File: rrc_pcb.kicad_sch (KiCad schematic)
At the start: 13 parts, among them J1 Conn_01x02_Male-Connector, J2 Conn_01x03_Male-Connector, U1 iridium9602, U2 Teensy4.1, U3 BN220-GPS, U4 ICM-20948, U5 MS5611, U6 logo

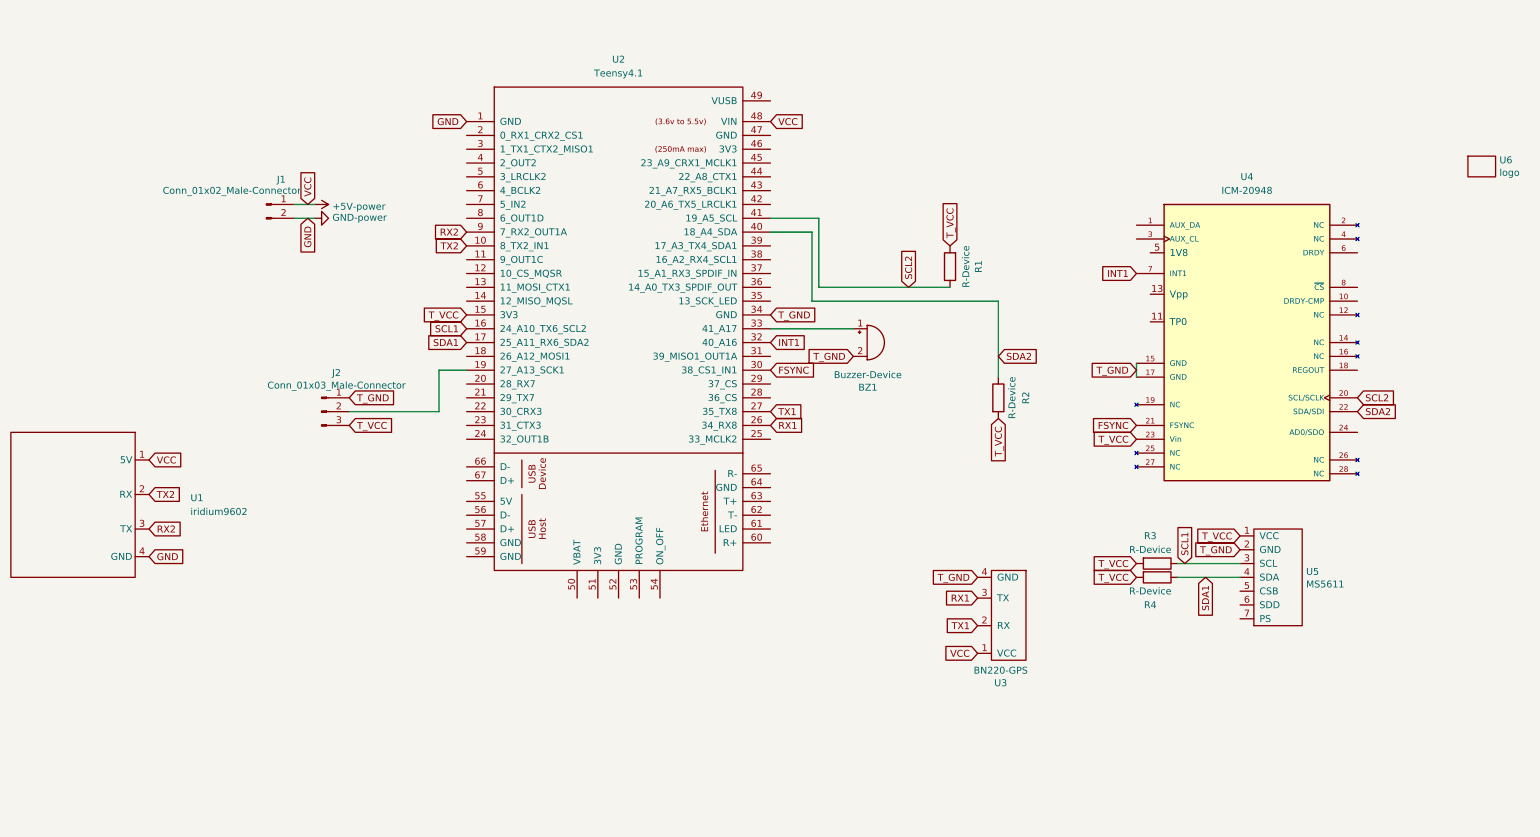
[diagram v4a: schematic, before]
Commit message: added edge cuts and mounting holes
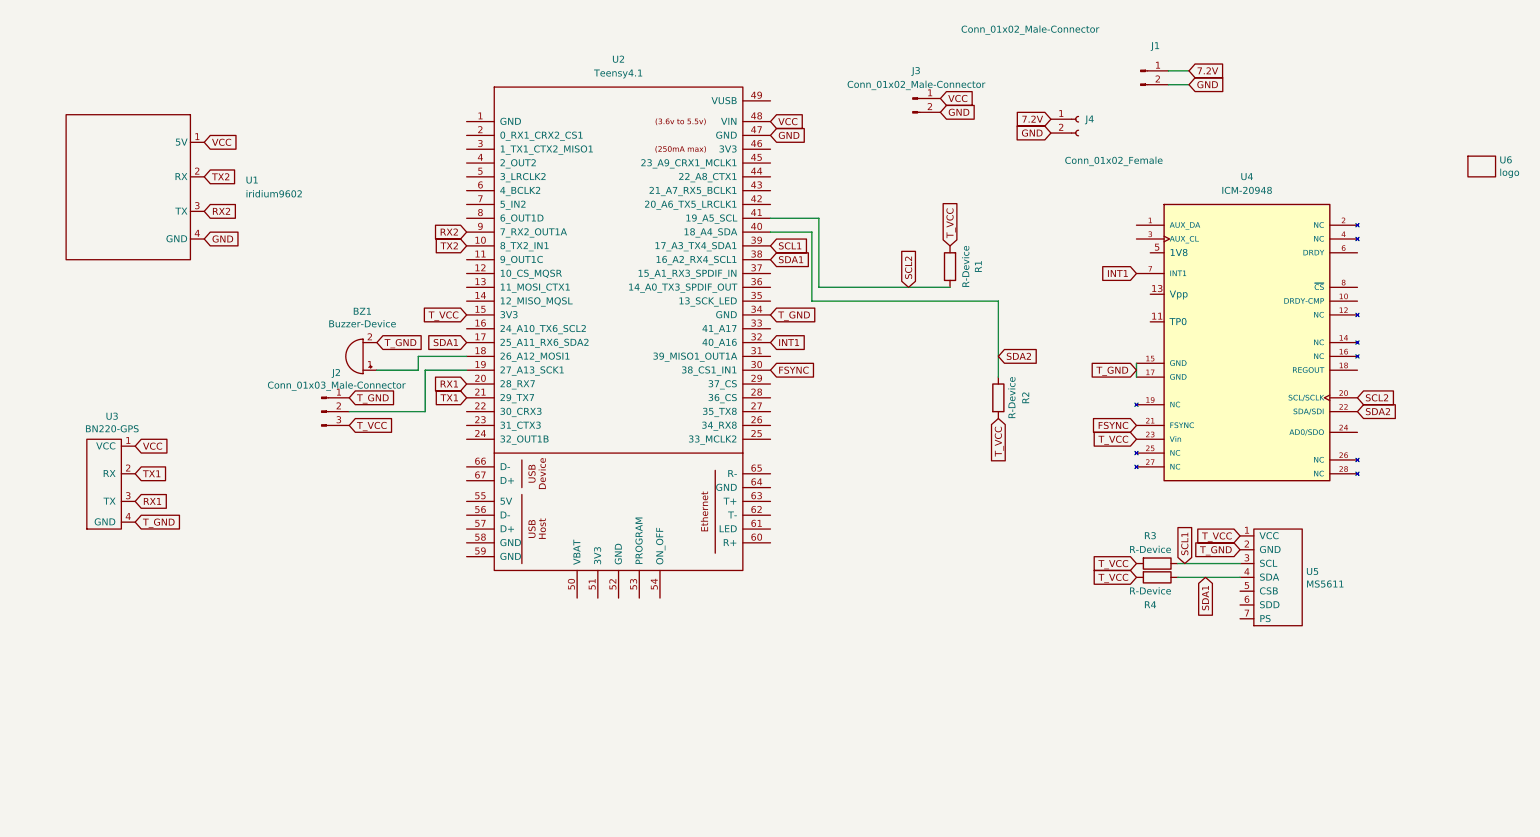
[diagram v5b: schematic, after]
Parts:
- added J3: Conn_01x02_Male-Connector, Connector_PinSocket_2.54mm:PinSocket_1x02_P2.54mm_Horizontal, symbol rrc_pcb-rescue:Conn_01x02_Male-Connector
- added J4: Conn_01x02_Female, Connector_PinSocket_2.54mm:PinSocket_2x01_P2.54mm_Horizontal, symbol Connector:Conn_01x02_Female
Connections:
- net GND: now also U2.47 (GND), J3.2 (Pin_2), J4.2 (Pin_2); no longer U2.1 (GND)
- net RX1: now also U2.20 (28_RX7); no longer U2.26 (34_RX8)
- net SCL1: now also U2.39 (17_A3_TX4_SDA1); no longer U2.16 (24_A10_TX6_SCL2)
- net SDA1: now also U2.38 (16_A2_RX4_SCL1)
- net TX1: now also U2.21 (29_TX7); no longer U2.27 (35_TX8)
- net at BZ1.1 (-): now also U2.18 (26_A12_MOSI1); no longer U2.33 (41_A17)
- net +5V renamed VCC
- net VCC: now also J3.1 (Pin_1); no longer J1.1 (Pin_1)
- new net 7.2V: J1.1 (Pin_1), J4.1 (Pin_1)
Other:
- moved on the sheet: BZ1, J1, U1, U3

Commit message: PCB is now ready to fabricate
added gerbers and traces
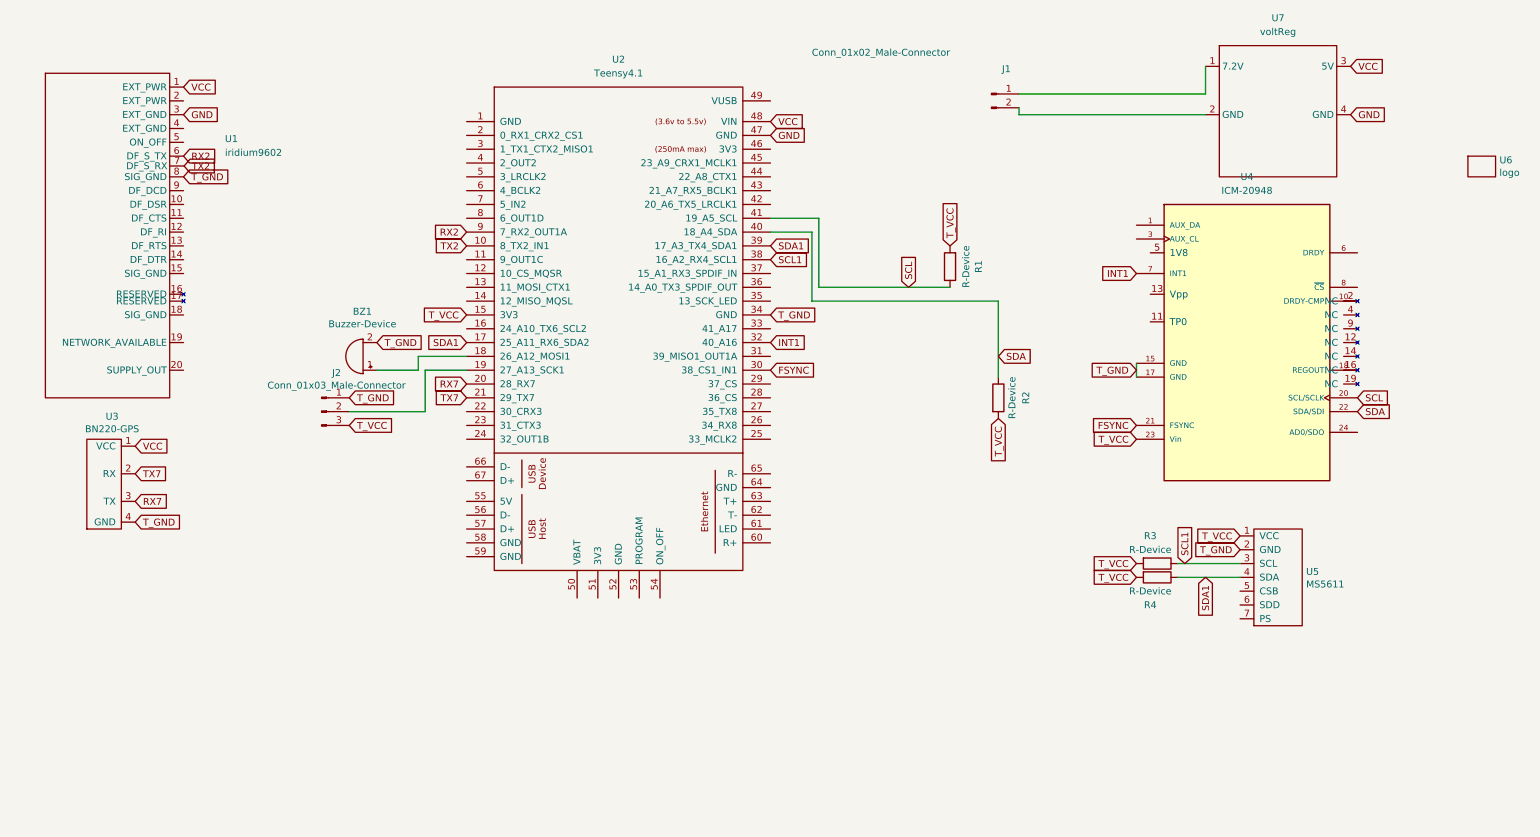
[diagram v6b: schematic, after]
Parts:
- removed J3: Conn_01x02_Male-Connector, Connector_PinSocket_2.54mm:PinSocket_1x02_P2.54mm_Horizontal, symbol rrc_pcb-rescue:Conn_01x02_Male-Connector
- removed J4: Conn_01x02_Female, Connector_PinSocket_2.54mm:PinSocket_2x01_P2.54mm_Horizontal, symbol Connector:Conn_01x02_Female
- added U7: voltReg, VoltReg:voltReg, symbol parts:voltReg
- U1: footprint Connector_PinHeader_2.54mm:PinHeader_1x04_P2.54mm_Horizontal -> iridium9602:iridium9602
- U3: footprint Connector_PinHeader_2.54mm:PinHeader_1x04_P2.54mm_Horizontal -> bn220_gps:BN220
- U4: footprint Connector_PinHeader_2.54mm:PinHeader_2x14_P2.54mm_Vertical -> icm20948:icm20948
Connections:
- net GND: now also U1.3 (EXT_GND), U7.4 (GND); no longer J1.2 (Pin_2), U1.4 (GND)
- net RX2: now also U1.6 (DF_S_TX); no longer U1.3 (TX)
- net SCL1: now also U2.38 (16_A2_RX4_SCL1); no longer U2.39 (17_A3_TX4_SDA1)
- net SDA1: now also U2.39 (17_A3_TX4_SDA1); no longer U2.38 (16_A2_RX4_SCL1)
- net TX2: now also U1.7 (DF_S_RX); no longer U1.2 (RX)
- net T_GND: now also U1.8 (SIG_GND)
- net VCC: now also U7.3 (5V)
- net at U4.10 (DRDY-CMP): now also U4.2 (NC)
- net at U4.16 (NC): now also U4.18 (REGOUT)
- net 7.2V: no longer names the net of J1.1 (Pin_1)
- net 7.2V: now also U7.1 (7.2V)
- net RX1 renamed RX7
- net SCL2 renamed SCL
- net SDA2 renamed SDA
- net TX1 renamed TX7
- new net: J1.2 (Pin_2), U7.2 (GND)
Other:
- moved on the sheet: J1
